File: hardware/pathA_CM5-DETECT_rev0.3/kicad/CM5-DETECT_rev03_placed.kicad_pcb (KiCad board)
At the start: 4 copper layers, 44 x 134 mm, 192 parts, among them M1 Raspberry Pi CM5 (CM5108032 /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

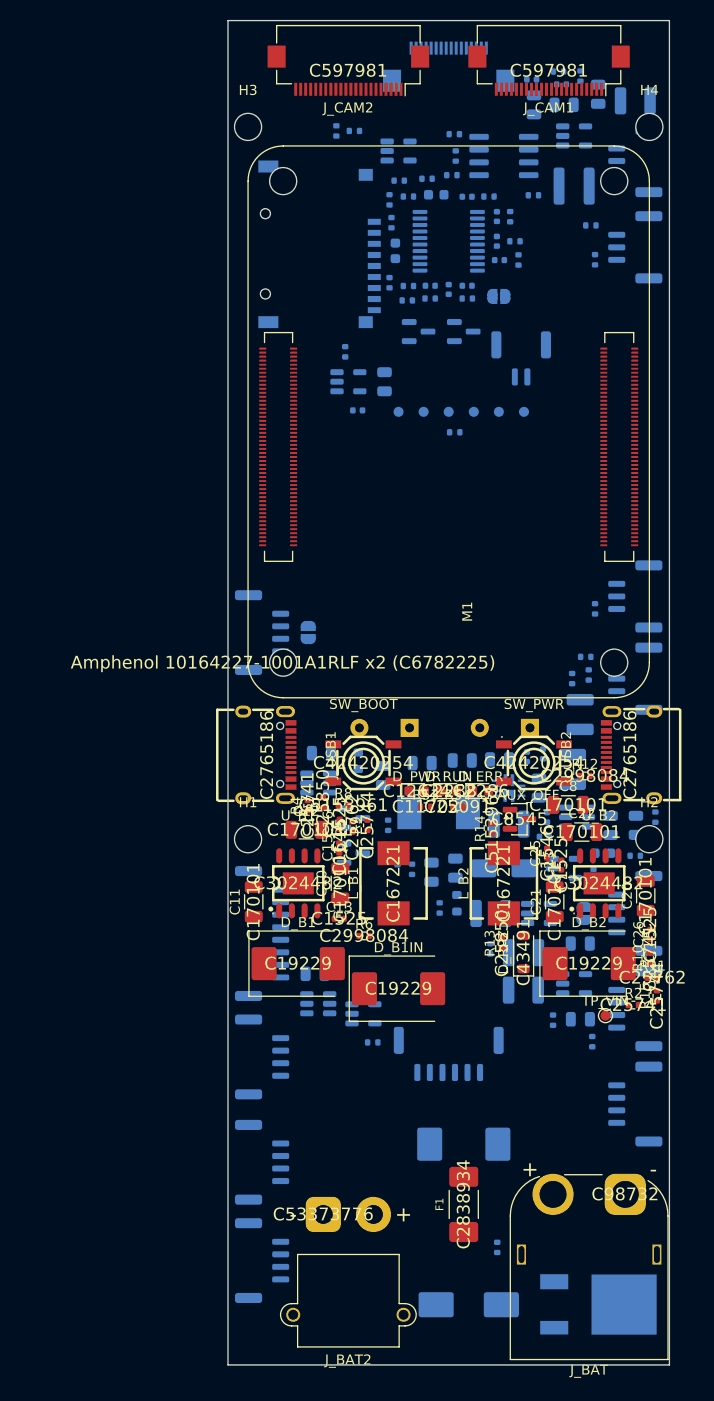
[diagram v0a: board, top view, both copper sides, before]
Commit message: rev0.3: placement fixes, 45-degree smoothing router, power pours, docs (functions, variants, cost), impedance calc
Co-Authored-By: Claude Opus 5.5 <noreply@anthropic.com>
Claude-Session: https://claude.ai/code/session_01QU2atnSo3eyX8zZazu88cn
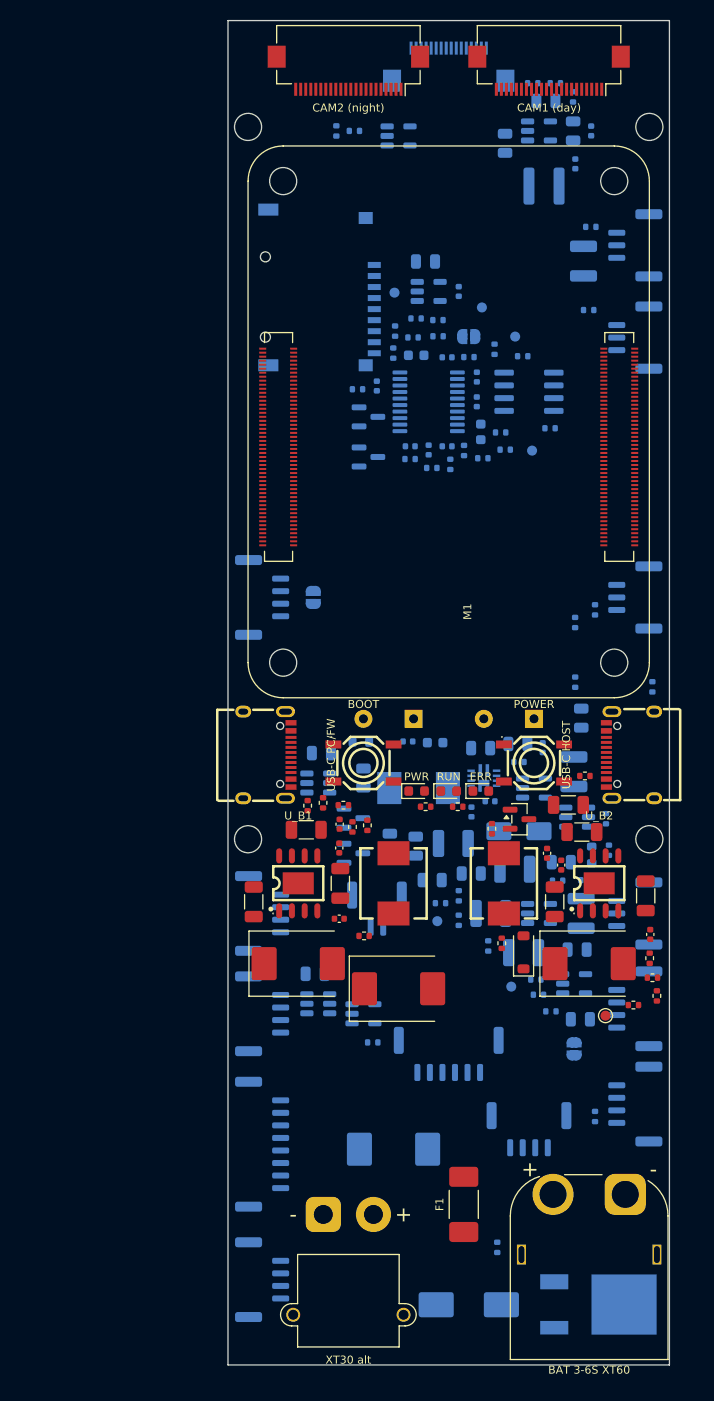
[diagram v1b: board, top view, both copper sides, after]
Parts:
- removed D_ERR: LED red ERROR, LED_0603_1608Metric
- removed D_PWR: LED green PWR, LED_0603_1608Metric
- removed D_RUN: LED blue RUN, LED_0603_1608Metric
- removed JP_MATEK: close = 5V to Matek pin1, SolderJumper-2_P1.3mm_Open_RoundedPad1.0x1.5mm
- removed JP_SERVO: close = servos from 5V_AUX (<=1.5 A tota, SolderJumper-2_P1.3mm_Open_RoundedPad1.0x1.5mm
- removed JP_WDT: close = watchdog disabled (bench), SolderJumper-2_P1.3mm_Open_RoundedPad1.0x1.5mm
- removed J_AIPWR: AI POWER 5V (5V,5V,GND,GND) for Hailo HA, JST_GH_SM04B-GHS-TB_1x04-1MP_P1.25mm_Horizontal
- removed J_BAT: XT60PW-M (battery 3S-6S), AMASS_XT60PW-M_1x02_P7.20mm_Horizontal
- removed J_BAT2: XT30PW-M (alternative input), AMASS_XT30PW-M_1x02_P2.50mm_Horizontal
- removed J_CAM1: CAM1 MIPI CSI-2 4-lane FFC 22p 0.5mm (Pi, Hirose_FH12-22S-0.5SH_1x22-1MP_P0.50mm_Horizontal
- removed J_CAM2: CAM2 MIPI CSI-2 4-lane FFC 22p 0.5mm (Pi, Hirose_FH12-22S-0.5SH_1x22-1MP_P0.50mm_Horizontal
- removed J_FAN: FAN 5V PWM (5V,PWM,GND,TACH), JST_GH_SM04B-GHS-TB_1x04-1MP_P1.25mm_Horizontal
- removed J_GPS: GPS/TELEM UART2 (5V,TX,RX,GND), JST_GH_SM04B-GHS-TB_1x04-1MP_P1.25mm_Horizontal
- removed J_I2C: I2C1 (3V3,SCL,SDA,GND), JST_GH_SM04B-GHS-TB_1x04-1MP_P1.25mm_Horizontal
- removed J_IO: GPIO (3V3,G7,G10,G11,G16,G17,G24,GND), JST_GH_SM08B-GHS-TB_1x08-1MP_P1.25mm_Horizontal
- removed J_MATEK: MATEK UART0 (5V*,TX,RX,GND), JST_GH_SM04B-GHS-TB_1x04-1MP_P1.25mm_Horizontal
- removed J_PCIE: PCIe x1 FFC 16p (Pi 5 pinout) -> Hailo A, Hirose_FH12-16S-0.5SH_1x16-1MP_P0.50mm_Horizontal
- removed J_RTC: RTC battery 3V (+,-), JST_GH_SM02B-GHS-TB_1x02-1MP_P1.25mm_Horizontal
- removed J_S1: SERVO1 (SIG,V+,GND), JST_GH_SM03B-GHS-TB_1x03-1MP_P1.25mm_Horizontal
- removed J_S2: SERVO2 (SIG,V+,GND), JST_GH_SM03B-GHS-TB_1x03-1MP_P1.25mm_Horizontal
- removed J_S3: SERVO3 (SIG,V+,GND), JST_GH_SM03B-GHS-TB_1x03-1MP_P1.25mm_Horizontal
- removed J_S4: SERVO4 (SIG,V+,GND), JST_GH_SM03B-GHS-TB_1x03-1MP_P1.25mm_Horizontal
- removed J_SD: microSD push-push TF-01A, TF-SMD_TF-01A
- removed J_SPWR: SERVO POWER IN from BEC (V+,V+,GND,GND), JST_GH_SM04B-GHS-TB_1x04-1MP_P1.25mm_Horizontal
- removed J_THA: THERMAL AUX (5V,3V3,SCL,SDA,SYNC,GND), JST_GH_SM06B-GHS-TB_1x06-1MP_P1.25mm_Horizontal
- removed J_THU: THERMAL USB (VBUS,D-,D+,GND), JST_GH_SM04B-GHS-TB_1x04-1MP_P1.25mm_Horizontal
- removed J_USB1: USB-C #1 FW/PC (rpiboot + USB gadget), USB-C-SMD_TYPE-C-16PIN-2MD-073
- removed J_USB2: USB-C #2 HOST, USB-C-SMD_TYPE-C-16PIN-2MD-073
- removed SW_BOOT: BOOT (nRPIBOOT), SW-SMD_4P-L5.2-W5.2-P3.70-LS6.4
- removed SW_PWR: POWER (PWR_BUT), SW-SMD_4P-L5.2-W5.2-P3.70-LS6.4
- added AI / Hailo PCIe: PCIe x1 FFC 16p (Pi 5 pinout) -> Hailo A, Hirose_FH12-16S-0.5SH_1x16-1MP_P0.50mm_Horizontal, B.Cu at (22.0, 4.60)
- added AI 5V: AI POWER 5V (5V,5V,GND,GND) for Hailo HA, JST_GH_SM04B-GHS-TB_1x04-1MP_P1.25mm_Horizontal, B.Cu at (30.0, 110.5)
- added BAT 3-6S XT60: XT60PW-M (battery 3S-6S), AMASS_XT60PW-M_1x02_P7.20mm_Horizontal, F.Cu at (39.6, 117.0)
- added BOOT: BOOT (nRPIBOOT), SW-SMD_4P-L5.2-W5.2-P3.70-LS6.4, F.Cu at (13.5, 74.0)
- added CAM1 (day): CAM1 MIPI CSI-2 4-lane FFC 22p 0.5mm (Pi, Hirose_FH12-22S-0.5SH_1x22-1MP_P0.50mm_Horizontal, F.Cu at (32.0, 5.00)
- added CAM2 (night): CAM2 MIPI CSI-2 4-lane FFC 22p 0.5mm (Pi, Hirose_FH12-22S-0.5SH_1x22-1MP_P0.50mm_Horizontal, F.Cu at (12.0, 5.00)
- added ERR: LED red ERROR, LED_0603_1608Metric, F.Cu at (25.2, 76.8)
- added FAN 5V: FAN 5V PWM (5V,PWM,GND,TACH), JST_GH_SM04B-GHS-TB_1x04-1MP_P1.25mm_Horizontal, B.Cu at (40.6, 108.0)
- added GPIO: GPIO (3V3,G7,G10,G11,G16,G17,G24,GND), JST_GH_SM08B-GHS-TB_1x08-1MP_P1.25mm_Horizontal, B.Cu at (3.40, 112.0)
- added GPS UART2: GPS/TELEM UART2 (5V,TX,RX,GND), JST_GH_SM04B-GHS-TB_1x04-1MP_P1.25mm_Horizontal, B.Cu at (3.40, 89.0)
- added I2C: I2C1 (3V3,SCL,SDA,GND), JST_GH_SM04B-GHS-TB_1x04-1MP_P1.25mm_Horizontal, B.Cu at (3.40, 99.0)
- added MATEK 5V: close = 5V to Matek pin1, SolderJumper-2_P1.3mm_Open_RoundedPad1.0x1.5mm, B.Cu at (8.50, 57.5)
- added MATEK UART0: MATEK UART0 (5V*,TX,RX,GND), JST_GH_SM04B-GHS-TB_1x04-1MP_P1.25mm_Horizontal, B.Cu at (3.40, 57.5)
- added POWER: POWER (PWR_BUT), SW-SMD_4P-L5.2-W5.2-P3.70-LS6.4, F.Cu at (30.5, 74.0)
- added PWR: LED green PWR, LED_0603_1608Metric, F.Cu at (18.8, 76.8)
- added RTC BAT: RTC battery 3V (+,-), JST_GH_SM02B-GHS-TB_1x02-1MP_P1.25mm_Horizontal, B.Cu at (14.8, 88.5)
- added RUN: LED blue RUN, LED_0603_1608Metric, F.Cu at (22.0, 76.8)
- added SERVO PWR (BEC): SERVO POWER IN from BEC (V+,V+,GND,GND), JST_GH_SM04B-GHS-TB_1x04-1MP_P1.25mm_Horizontal, B.Cu at (40.6, 98.5)
- added SERVO1: SERVO1 (SIG,V+,GND), JST_GH_SM03B-GHS-TB_1x03-1MP_P1.25mm_Horizontal, B.Cu at (40.6, 22.4)
- added SERVO2: SERVO2 (SIG,V+,GND), JST_GH_SM03B-GHS-TB_1x03-1MP_P1.25mm_Horizontal, B.Cu at (40.6, 31.6)
- added SERVO3: SERVO3 (SIG,V+,GND), JST_GH_SM03B-GHS-TB_1x03-1MP_P1.25mm_Horizontal, B.Cu at (40.6, 57.5)
- added SERVO4: SERVO4 (SIG,V+,GND), JST_GH_SM03B-GHS-TB_1x03-1MP_P1.25mm_Horizontal, B.Cu at (40.6, 89.0)
- added SERVO=5V: close = servos from 5V_AUX (<=1.5 A tota, SolderJumper-2_P1.3mm_Open_RoundedPad1.0x1.5mm, B.Cu at (34.5, 102.5)
- added THERMAL AUX: THERMAL AUX (5V,3V3,SCL,SDA,SYNC,GND), JST_GH_SM06B-GHS-TB_1x06-1MP_P1.25mm_Horizontal, B.Cu at (22.0, 103.0)
- added THERMAL USB: THERMAL USB (VBUS,D-,D+,GND), JST_GH_SM04B-GHS-TB_1x04-1MP_P1.25mm_Horizontal, B.Cu at (3.40, 125.5)
- added USB-C HOST: USB-C #2 HOST, USB-C-SMD_TYPE-C-16PIN-2MD-073, F.Cu at (40.1, 73.2)
- added USB-C PC/FW: USB-C #1 FW/PC (rpiboot + USB gadget), USB-C-SMD_TYPE-C-16PIN-2MD-073, F.Cu at (3.90, 73.2)
- added WDT OFF: close = watchdog disabled (bench), SolderJumper-2_P1.3mm_Open_RoundedPad1.0x1.5mm, B.Cu at (24.0, 31.5)
- added XT30 alt: XT30PW-M (alternative input), AMASS_XT30PW-M_1x02_P2.50mm_Horizontal, F.Cu at (9.50, 119.0)
- added microSD: microSD push-push TF-01A, TF-SMD_TF-01A, B.Cu at (9.30, 26.6)
- moved TP_5VA 57.3 mm to (28.2, 96.3)
- moved TP_5V 51.1 mm to (20.9, 89.8)
- moved R60 34.0 mm to (30.9, 97.1)
- moved R52 30.8 mm to (32.1, 40.6)
- moved R55 28.8 mm to (27.6, 42.8)
- moved R47 27.7 mm to (23.0, 89.7)
- moved R40 27.6 mm to (20.3, 44.6)
- moved C4 27.6 mm to (13.5, 75.5)
- moved R39 27.0 mm to (22.2, 44.2), turned to 90 degrees
- moved R23 25.9 mm to (21.2, 88.0), turned to 0 degrees
- moved R24 25.0 mm to (34.6, 65.9)
- moved U_TEMP 23.6 mm to (30.0, 37.0)
- moved R44 23.3 mm to (12.9, 36.7)
- moved R_VREF 22.4 mm to (34.6, 60.0), turned to 90 degrees
- moved R45 21.5 mm to (27.2, 41.1), turned to 0 degrees
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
